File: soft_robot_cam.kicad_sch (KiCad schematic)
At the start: 53 parts, among them J1 Conn_01x24_Socket, J2 Screw_Terminal_01x02, J3 Screw_Terminal_01x02, J5 Connector, J6 Conn_01x04, J7 Conn_01x06, J9 Conn_01x03, Q1 S8050, Q2 S8050, Q3 AO3401A, SW3 SW_Push, SW5 SW_Push, U1 DRV8872DDA, U10 ICM-42605, U12 XC6206P282MR, U13 XC6206P122MR, U14 SY8113IADC, U2 DRV8872DDA, U3 MPU6500, U4 INA180A3, U9 ESP32-S3-WROOM-1-N16R8

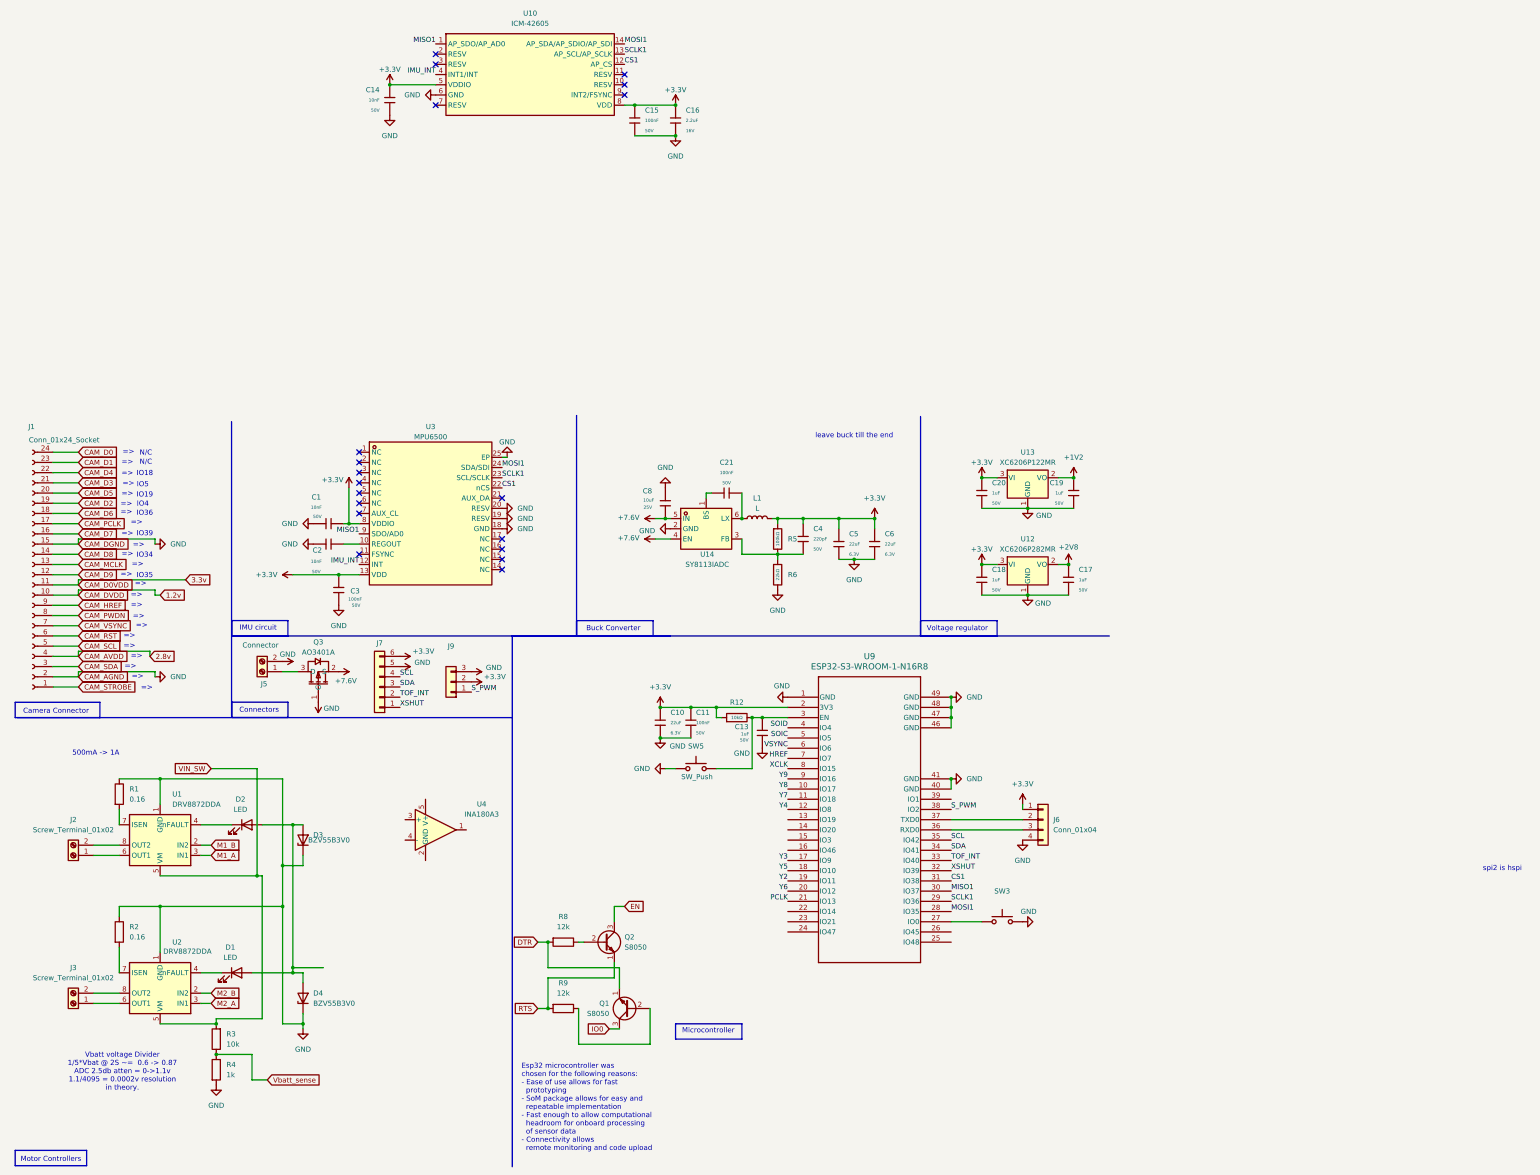
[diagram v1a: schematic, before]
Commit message: Completed the schematic, began layout
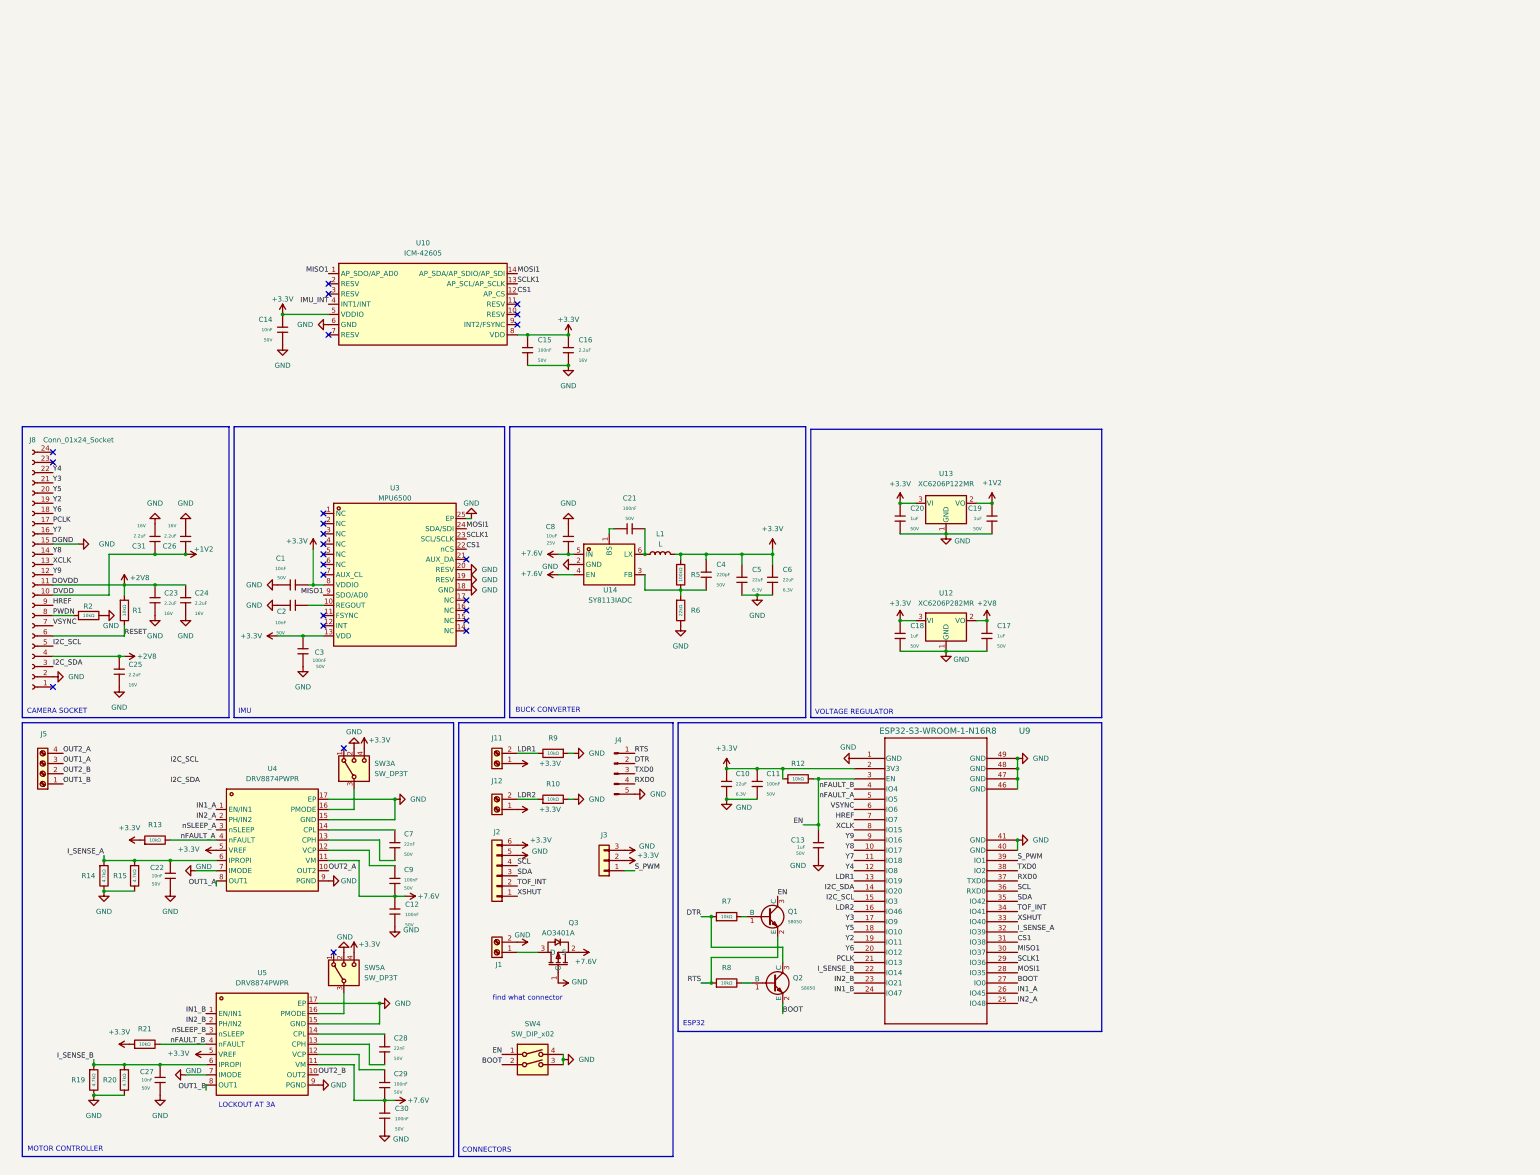
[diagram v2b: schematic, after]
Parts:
- removed D1, D2: LED, LED_SMD:LED_0603_1608Metric, symbol Device:LED
- removed D3, D4: BZV55B3V0, Diode_SMD:D_MiniMELF_Handsoldering, symbol Diode:BZV55B3V0
- removed J1: Conn_01x24_Socket, Connector_FFC-FPC:Hirose_FH12-24S-0.5SH_1x24-1MP_P0.50mm_Horizontal, symbol Connector:Conn_01x24_Socket
- removed J2, J3: Screw_Terminal_01x02, Connector_PinSocket_2.54mm:PinSocket_1x02_P2.54mm_Horizontal, symbol Connector:Screw_Terminal_01x02
- removed J6: Conn_01x04, symbol Connector_Generic:Conn_01x04
- removed Q1, Q2: S8050, Package_TO_SOT_THT:TO-92_Inline, symbol Transistor_BJT:S8050
- removed R1, R2: 0.16, PCM_Resistor_SMD_AKL:R_0805_2012Metric_Pad1.15x1.40mm_HandSolder, symbol Device:R
- removed R3: 10k, PCM_Resistor_SMD_AKL:R_0805_2012Metric_Pad1.15x1.40mm_HandSolder, symbol Device:R
- removed R4: 1k, PCM_Resistor_SMD_AKL:R_0805_2012Metric_Pad1.15x1.40mm_HandSolder, symbol Device:R
- removed R8, R9: 12k, PCM_Resistor_SMD_AKL:R_0805_2012Metric_Pad1.15x1.40mm_HandSolder, symbol Device:R
- removed SW3, SW5: SW_Push, symbol Switch:SW_Push
- removed U1, U2: DRV8872DDA, Package_SO:Texas_HTSOP-8-1EP_3.9x4.9mm_P1.27mm_EP2.95x4.9mm_Mask2.4x3.1mm_ThermalVias, symbol Driver_Motor:DRV8872DDA
- removed U4: INA180A3, Package_TO_SOT_SMD:SOT-23-5, symbol Amplifier_Current:INA180A3
- added C12, C29, C30, C9: 100nF, PCM_JLCPCB:C_0603, symbol PCM_JLCPCB-Capacitors:0603,100nF
- added C22, C27: 10nF, PCM_JLCPCB:C_0603, symbol PCM_JLCPCB-Capacitors:0603,10nF
- added C23, C24, C25, C26, C31: 2.2uF, PCM_JLCPCB:C_0603, symbol PCM_JLCPCB-Capacitors:0603,2.2uF
- added C28, C7: 22nF, PCM_JLCPCB:C_0603, symbol PCM_JLCPCB-Capacitors:0603,22nF
- added J11, J12: Screw_Terminal_01x02, PRETTY:CONN-TH_B2B-PH-K-S, symbol Connector:Screw_Terminal_01x02
- added J4: Conn_01x05_Pin, Connector_PinHeader_1.27mm:PinHeader_1x05_P1.27mm_Vertical, symbol Connector:Conn_01x05_Pin
- added J5: Screw_Terminal_01x04, PRETTY:CONN-TH_4P-P2.54_MX128-2.54-GN01-04P-CU-Y-A, symbol Connector:Screw_Terminal_01x04
- added J8: Conn_01x24_Socket, Connector_FFC-FPC:Hirose_FH12-24S-0.5SH_1x24-1MP_P0.50mm_Horizontal, symbol Connector:Conn_01x24_Socket
- added Q1, Q2: S8050, PCM_JLCPCB:Q_SOT-23, symbol PCM_JLCPCB-Transistors:NPN,S8050
- added R1, R10, R13, R2, R21, R7, R8, R9: 10kΩ, PCM_JLCPCB:R_0603, symbol PCM_JLCPCB-Resistors:0603,10kΩ
- added R14, R15, R19, R20: 4.7kΩ, PCM_JLCPCB:R_0603, symbol PCM_JLCPCB-Resistors:0603,4.7kΩ
- added SW3, SW5: SW_DP3T, symbol Switch:SW_DP3T
- added SW4: SW_DIP_x02, easyeda2kicad:SW-SMD_4P_DSHP02TSGET, symbol Switch:SW_DIP_x02
- added U4, U5: DRV8874PWPR, easyeda2kicad:HTSSOP-16_L5.0-W4.4-P0.65-LS6.4-BL-EP, symbol easyeda2kicad:DRV8874PWPR
- J1: renamed from J5; footprint Connector_Wire:SolderWire-1sqmm_1x02_P5.4mm_D1.4mm_OD2.7mm -> Connector_AMASS:AMASS_XT30U-F_1x02_P5.0mm_Vertical
- J2: renamed from J7; footprint (none) -> easyeda2kicad:CONN-TH_B6B-PH-K-S; LCSC (none) -> C131342
- J3: renamed from J9; footprint (none) -> easyeda2kicad:CONN-TH_3P-P2.50_A2501WV2-3P; LCSC (none) -> C144394
- U3: footprint easyeda2kicad:QFN-24_L3.0-W3.0-P0.40-BL-EP -> Package_DFN_QFN:QFN-24-1EP_3x3mm_P0.4mm_EP1.75x1.6mm
- U9: footprint ESP32-S3-WROOM-1_EXP -> esp32:ESP32-S3-WROOM-1_EXP
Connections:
- net +1V2: now also C26.1, C31.1, J8.10 (Pin_10)
- net +2V8: now also C23.1, C24.1, C25.1, J8.11 (Pin_11), J8.4 (Pin_4), R1.1
- net +3.3V: now also J11.1 (Pin_1), J12.1 (Pin_1), R13.1, R21.1, SW3.4, SW5.4, U4.5 (VREF), U5.5 (VREF)
- net +7.6V: now also C12.1, C29.2, C30.1, C9.2, U4.11 (VM), U5.11 (VM)
- net DTR: now also J4.2 (Pin_2), Q2.3 (C), R7.1
- net EN: now also C13.1, R12.2, U9.3 (EN), Q1.3 (C), SW4.1
- net GND: now also C12.2, C22.1, C23.2, C24.2, C25.2, C26.2, C27.1, C30.2, C31.2, J4.5 (Pin_5), J8.15 (Pin_15), J8.2 (Pin_2), R10.2, R14.2, R15.2, R19.2, R2.2, R20.2, R9.1, SW3.2, SW4.3, SW4.4, SW5.2, U4.15 (GND), U4.17 (EP), U4.7 (IMODE), U4.9 (PGND), U5.15 (GND), U5.17 (EP), U5.7 (IMODE), U5.9 (PGND)
- net HREF: now also J8.9 (Pin_9)
- net IMU_INT: no longer U3.12 (INT)
- net PCLK: now also J8.17 (Pin_17)
- net RTS: now also J4.1 (Pin_1), Q1.2 (E), R8.1
- net SCL: now also U9.36 (RXD0); no longer U9.35 (IO42)
- net SDA: now also U9.35 (IO42); no longer U9.34 (IO41)
- net S_PWM: now also U9.39 (IO1); no longer U9.38 (IO2)
- net TOF_INT: now also U9.34 (IO41); no longer U9.33 (IO40)
- net VSYNC: now also J8.7 (Pin_7)
- net XCLK: now also J8.13 (Pin_13)
- net XSHUT: now also U9.33 (IO40); no longer U9.32 (IO39)
- net Y2: now also J8.19 (Pin_19)
- net Y3: now also J8.21 (Pin_21)
- net Y4: now also J8.22 (Pin_22)
- net Y5: now also J8.20 (Pin_20)
- net Y6: now also J8.18 (Pin_18)
- net Y7: now also J8.16 (Pin_16)
- net Y8: now also J8.14 (Pin_14)
- net Y9: now also J8.12 (Pin_12)
- net BOOT: now reaches U9.27 (IO0)
- net BOOT: now also Q2.2 (E), SW4.2
- net LDR1: now reaches U9.13 (IO19)
- net LDR1: now also J11.2 (Pin_2), R9.2
- net I2C_SDA: now reaches U9.14 (IO20)
- net I2C_SDA: now also J8.3 (Pin_3)
- net I2C_SCL: now reaches U9.15 (IO3)
- net I2C_SCL: now also J8.5 (Pin_5)
- net LDR2: now reaches U9.16 (IO46)
- net LDR2: now also J12.2 (Pin_2), R10.1
- net I_SENSE_B: now reaches U9.22 (IO14)
- net I_SENSE_B: now also C27.2, R19.1, R20.1, U5.6 (IPROPI)
- net IN2_B: now reaches U9.23 (IO21)
- net IN2_B: now also U5.2 (PH/IN2)
- net IN1_B: now reaches U9.24 (IO47)
- net IN1_B: now also U5.1 (EN/IN1)
- net IN2_A: now reaches U9.25 (IO48)
- net IN2_A: now also U4.2 (PH/IN2)
- net IN1_A: now reaches U9.26 (IO45)
- net IN1_A: now also U4.1 (EN/IN1)
- net RXD0: now reaches U9.37 (TXD0)
- net RXD0: now also J4.4 (Pin_4)
- net SOIC renamed nFAULT_A
- net nFAULT_A: now also R13.2, U4.4 (nFAULT)
- net SOID renamed nFAULT_B
- net nFAULT_B: now also R21.2, U5.4 (nFAULT)
- new net: C29.1, U5.12 (VCP)
- new net: Q1.1 (B), R7.2
- new net: Q2.1 (B), R8.2
- new net: C9.1, U4.12 (VCP)
- new net: C7.2, U4.13 (CPH)
- new net: C7.1, U4.14 (CPL)
- new net: SW3.3, U4.16 (PMODE)
- new net: C28.1, U5.14 (CPL)
- new net: C28.2, U5.13 (CPH)
- new net: SW5.3, U5.16 (PMODE)
- new net I_SENSE_A: C22.2, R14.1, R15.1, U4.6 (IPROPI), U9.32 (IO39)
- new net OUT1_A: J5.3 (Pin_3), U4.8 (OUT1)
- new net OUT1_B: J5.1 (Pin_1), U5.8 (OUT1)
- new net OUT2_A: J5.4 (Pin_4), U4.10 (OUT2)
- new net OUT2_B: J5.2 (Pin_2), U5.10 (OUT2)
- new net PWDN: J8.8 (Pin_8), R2.1
- new net RESET: J8.6 (Pin_6), R1.2
- new net TXD0: J4.3 (Pin_3), U9.38 (IO2)
- new net nSLEEP_A: U4.3 (nSLEEP)
- new net nSLEEP_B: U5.3 (nSLEEP)
- no-connect marks 19 -> 25
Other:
- note added: "BUCK CONVERTER"
- note added: "CAMERA SOCKET"
- note added: "CONNECTORS"
- note added: "ESP32"
- note added: "IMU"
- note added: "LOCKOUT AT 3A"
- note added: "MOTOR CONTROLLER"
- note added: "VOLTAGE REGULATOR"
- note added: "find what connector"
- note removed: "500mA -> 1A"
- note removed: "=>"
- note removed: "Buck Converter"
- note removed: "Camera Connector"
- note removed: "Connectors"
- note removed: "Esp32 microcontroller was chosen for the following reasons: - Ease of use allows for fast prototyping - SoM package allows for easy and repeatable implementation - Fast enough to allow computational headroom for onboard processing of sensor data - Connectivity allows remote monitoring and code upload"
- note removed: "IMU circuit"
- note removed: "IO18"
- note removed: "IO19"
- note removed: "IO34"
- note removed: "IO35"
- note removed: "IO36"
- note removed: "IO39"
- note removed: "IO4"
- note removed: "IO5"
- note removed: "Microcontroller"
- note removed: "Motor Controllers"
- note removed: "N/C"
- note removed: "Vbatt voltage Divider 1/5*Vbat @ 2S ~= 0.6 -> 0.87 ADC 2.5db atten = 0->1.1v 1.1/4095 = 0.0002v resolution in theory."
- note removed: "Voltage regulator"
- note removed: "leave buck till the end"
- note removed: "spi2 is hspi"
- moved on the sheet: C1, C10, C11, C13, C14, C15, C16, C17, C18, C19, C2, C20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

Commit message: Restitched old board, last version with old board attached, finalized layout aside from PMODE connectors.
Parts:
- removed J11, J12: Screw_Terminal_01x02, PRETTY:CONN-TH_B2B-PH-K-S, symbol Connector:Screw_Terminal_01x02
- removed L1: L, symbol Device:L
- added C32: 10uF, PCM_JLCPCB:C_0603, symbol PCM_JLCPCB-Capacitors:0603,10uF,(2)
- added C33: 22uF, PCM_JLCPCB:C_0603, symbol PCM_JLCPCB-Capacitors:0603,22uF
- added C34, C35: 10uF, PCM_JLCPCB:C_1206, symbol PCM_JLCPCB-Capacitors:1206,10uF
- added J10, J6, J7, J9: Screw_Terminal_01x02, easyeda2kicad:CONN-TH_B2B-PH-K-S, symbol Connector:Screw_Terminal_01x02
- added L2: SRN6045-6R8Y, easyeda2kicad:IND-SMD_L6.0-W6.0_SRN6045, symbol easyeda2kicad:SRN6045-6R8Y
- added SW1: SW_DIP_x02, easyeda2kicad:SW-SMD_4P_DSHP02TSGET, symbol Switch:SW_DIP_x02
- J2: footprint easyeda2kicad:CONN-TH_B6B-PH-K-S -> easyeda2kicad:JST_B6B-PH-K-S
- J3: footprint easyeda2kicad:CONN-TH_3P-P2.50_A2501WV2-3P -> easyeda2kicad:JST_B3B-PH-K-S; LCSC C144394 -> C131339
- U3: footprint Package_DFN_QFN:QFN-24-1EP_3x3mm_P0.4mm_EP1.75x1.6mm -> easyeda2kicad:QFN40P300X300X95-25N
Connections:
- net +3.3V: now also J2.5 (Pin_5), C33.1, J10.2 (Pin_2), J9.1 (Pin_1), L2.2; no longer J2.6 (Pin_6)
- net +7.6V: now also C32.2, C34.1, C35.1
- net BOOT: now also SW4.1; no longer SW4.2
- net EN: now also SW4.2; no longer SW4.1
- net GND: now also J1.1 (Pin_1), J2.6 (Pin_6), C32.1, C33.2, C34.2, C35.2, SW1.3, SW1.4; no longer J1.2 (Pin_2), J2.5 (Pin_5)
- net I2C_SCL: now also U9.16 (IO46); no longer U9.15 (IO3)
- net I2C_SDA: now also U9.15 (IO3); no longer U9.14 (IO20)
- net I_SENSE_A: now also U9.22 (IO14); no longer U9.32 (IO39)
- net I_SENSE_B: now also U9.32 (IO39); no longer U9.22 (IO14)
- net LDR1: now also J9.2 (Pin_2)
- net LDR2: now also U9.14 (IO20), J10.1 (Pin_1); no longer U9.16 (IO46)
- net OUT1_A: now also J6.1 (Pin_1)
- net OUT1_B: now also J7.1 (Pin_1)
- net OUT2_A: now also J6.2 (Pin_2)
- net OUT2_B: now also J7.2 (Pin_2)
- net nSLEEP_A: now also SW1.1
- net nSLEEP_B: now also SW1.2
- net at Q3.3 (D): now also J1.2 (Pin_2); no longer J1.1 (Pin_1)
- net at C21.2, U14.6 (LX): now also L2.1
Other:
- note added: "XT30U-F"
- note removed: "find what connector"
- moved on the sheet: C21, C4, C5, C6, C8, J1, Q3, R10, R5, R6, SW4, U14
